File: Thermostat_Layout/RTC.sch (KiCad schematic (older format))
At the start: 2 parts, among them U5 DS3231MZ

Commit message: Update schematic
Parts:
- renumbered U5 to U9
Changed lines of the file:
@@
 $EndDescr
 $Comp
-L Timer_RTC:DS3231MZ U5
+L Timer_RTC:DS3231MZ U9
 U 1 1 5D3F90D1
 P 5750 3150
-F 0 "U5" H 5750 2661 50  0000 C CNN
+F 0 "U9" H 5750 2661 50  0000 C CNN
 F 1 "DS3231MZ" H 5750 2570 50  0000 C CNN
 F 2 "Package_SO:SOIC-8_3.9x4.9mm_P1.27mm" H 5750 2650 50  0001 C CNN
@@
 $EndComp
 $Comp
-L SparkFun-PowerSymbols:GND #GND0109
+L SparkFun-PowerSymbols:GND #GND015
 U 1 1 5D3F958C
 P 5750 3850
-F 0 "#GND0109" H 5800 3800 45  0001 L BNN
+F 0 "#GND015" H 5800 3800 45  0001 L BNN
 F 1 "GND" H 5750 3680 45  0000 C CNN
 F 2 "" H 5750 3750 60  0001 C CNN
@@
 $EndComp
 $Comp
-L SparkFun-PowerSymbols:3.3V #SUPPLY0106
+L SparkFun-PowerSymbols:3.3V #SUPPLY08
 U 1 1 5D3F99F0
 P 5750 2550
-F 0 "#SUPPLY0106" H 5800 2550 45  0001 L BNN
+F 0 "#SUPPLY08" H 5800 2550 45  0001 L BNN
 F 1 "3.3V" H 5750 2826 45  0000 C CNN
 F 2 "XXX-00000" H 5750 2731 60  0000 C CNN

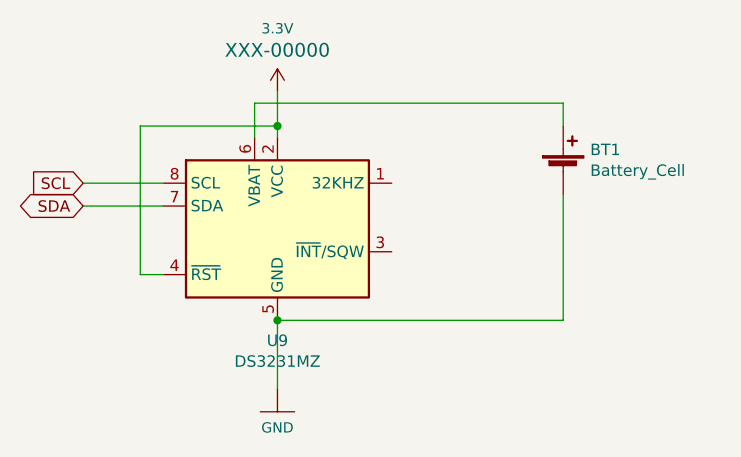
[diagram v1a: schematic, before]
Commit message: FInalize schematic for thermostat
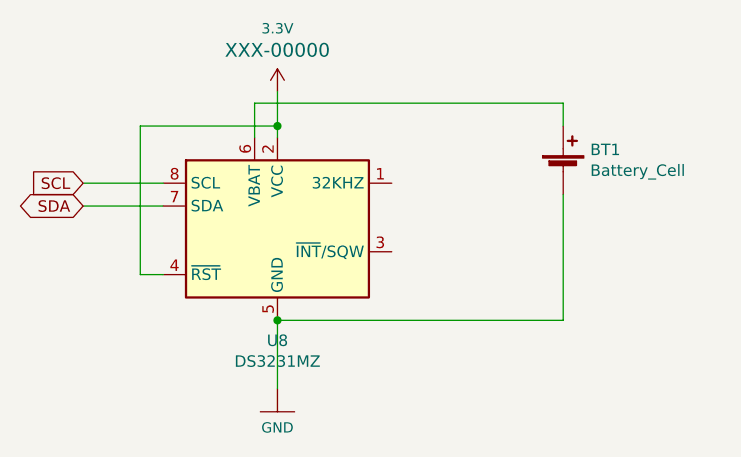
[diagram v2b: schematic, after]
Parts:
- renumbered U9 to U8
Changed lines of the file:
@@
 $EndDescr
 $Comp
-L Timer_RTC:DS3231MZ U9
+L Timer_RTC:DS3231MZ U8
 U 1 1 5D3F90D1
 P 5750 3150
-F 0 "U9" H 5750 2661 50  0000 C CNN
+F 0 "U8" H 5750 2661 50  0000 C CNN
 F 1 "DS3231MZ" H 5750 2570 50  0000 C CNN
 F 2 "Package_SO:SOIC-8_3.9x4.9mm_P1.27mm" H 5750 2650 50  0001 C CNN
@@
 $EndComp
 $Comp
-L SparkFun-PowerSymbols:GND #GND015
+L SparkFun-PowerSymbols:GND #GND013
 U 1 1 5D3F958C
 P 5750 3850
-F 0 "#GND015" H 5800 3800 45  0001 L BNN
+F 0 "#GND013" H 5800 3800 45  0001 L BNN
 F 1 "GND" H 5750 3680 45  0000 C CNN
 F 2 "" H 5750 3750 60  0001 C CNN
@@
 $EndComp
 $Comp
-L SparkFun-PowerSymbols:3.3V #SUPPLY08
+L SparkFun-PowerSymbols:3.3V #SUPPLY07
 U 1 1 5D3F99F0
 P 5750 2550
-F 0 "#SUPPLY08" H 5800 2550 45  0001 L BNN
+F 0 "#SUPPLY07" H 5800 2550 45  0001 L BNN
 F 1 "3.3V" H 5750 2826 45  0000 C CNN
 F 2 "XXX-00000" H 5750 2731 60  0000 C CNN
